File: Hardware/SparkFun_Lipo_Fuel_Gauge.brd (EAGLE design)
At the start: 10.2 x 24.1 mm, 17 parts, among them U2 MAX1704X

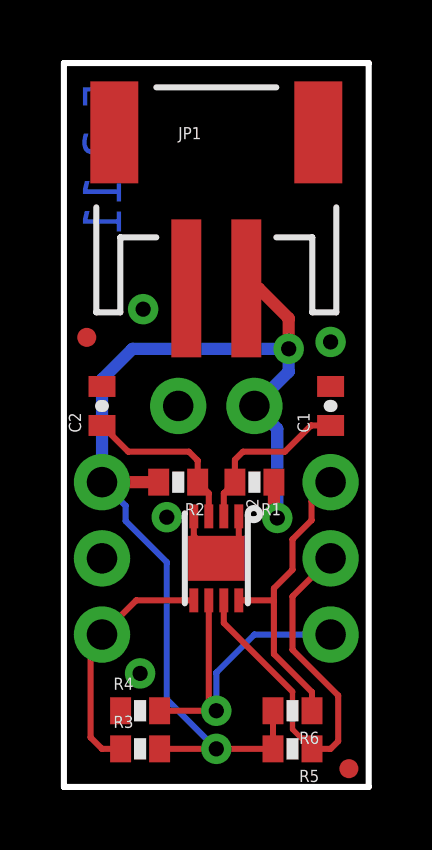
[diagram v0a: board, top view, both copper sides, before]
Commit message: Revision updates
Purpose of revision:
VCC connects directly to battery, which means a user could connect a 3V3 signal to 4V2 of the battery, causing things to break (see latest 1-star review on product page). This revision is to separate VCC from V_BATT, allowing users to use any voltage for the logic side. Also update to latest standards while we're at it.

Schematic changes:
Add Revised By
Update revision number
Replace VCC on battery side with V_BATT symbol
Separate regions of circuit
Add dashed lines to distinguish circuit regions
Separate JP1 and JP5
Replace schematic frame with current version
Replace "SFE" symbol with SparkFun logo
Move C2 to connect to VDD directly
Change flags to vector font
Change flags to correct types
Replace fiducials with new version

Board changes:
Add measures
Change copper date to version number
Add battery +/- labels to top silk
Add fiducials to bottom
Decrease GND pour isolation from 12mil to 8mil
Decrease all vias from 20 mil to 15 mil
Approve DRC keepout errors
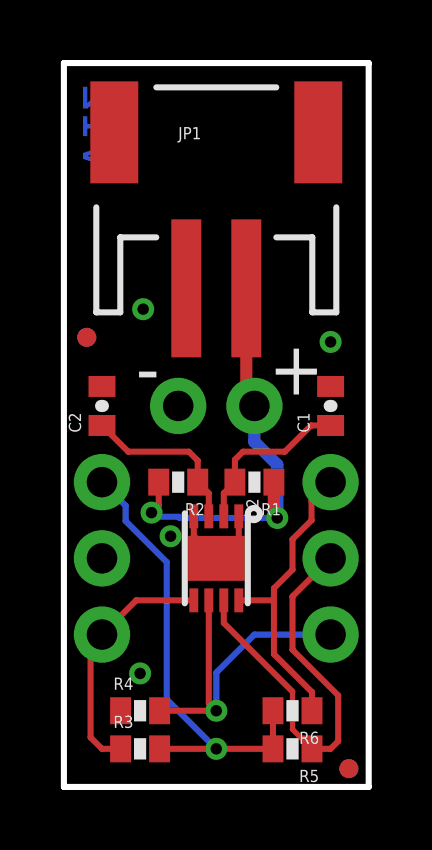
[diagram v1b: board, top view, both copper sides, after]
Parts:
- added FRAME1: FRAME-LETTER, SparkFun-Aesthetics:CREATIVE_COMMONS
- added JP8, JP9: FIDUCIALUFIDUCIAL, SparkFun-Aesthetics:FIDUCIAL-MICRO
- added LOGO1: SFE_LOGO_NAME_FLAMEBLANK, SparkFun-Aesthetics:BLANK
- JP3: value LOGO-SFESK -> SFE_LOGO_FLAME.1_INCH; device SparkFun:SFE-LOGO-FLAME -> SparkFun-Aesthetics:SFE_LOGO_FLAME_.1
- JP6, JP7: value FIDUCIAL1X2.5 -> FIDUCIALUFIDUCIAL; device abes:FIDUCIAL-1X2.5 -> SparkFun-Aesthetics:FIDUCIAL-MICRO
- moved JP3 1.66 mm to (5.08, 18.7)
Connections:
- new net V_BATT: JP1.2, JP5.1, R1.1, R2.2
- net VCC: no longer JP1.2, JP5.1, R1.1, R2.2
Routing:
- net VCC: track 38.1 -> 15.5 mm, vias 3 -> 1
- net V_BATT: track 0.00 -> 14.7 mm, vias 0 -> 2
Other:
- board text added: "Aaron Weiss"
- board text added: "Dryw Wade"
- board text added: "Revised by:"
- board text added: "v12"
- board text removed: "5-3-11"

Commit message: Design review updates
Schematic:
Replace old Eagle devices with current ones
Update MAX1704X symbol to match current standards
Add warning about single cell LiPo only
Add voltage range for V_BATT and VCC
Add I2C pullup isolation jumper

Board:
Fix routing with new footprints
Route straight out of all pads
Add vias to increase GND pour
Switch to Buzzard silk labels
Add units to measures
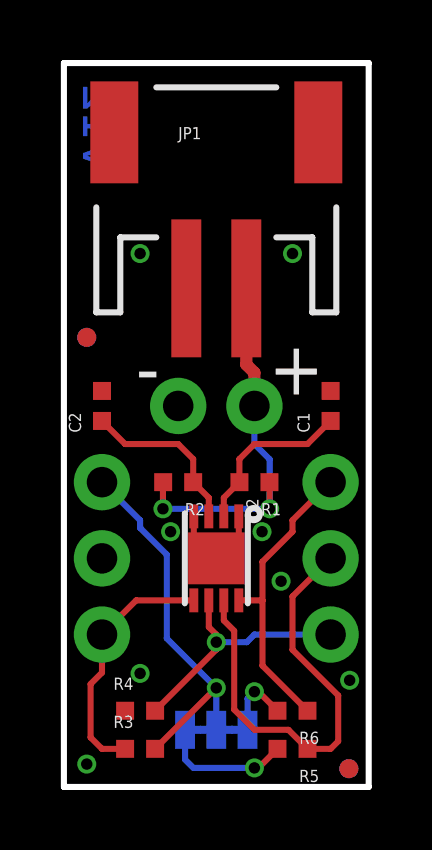
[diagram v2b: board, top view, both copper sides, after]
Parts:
- added I2C: JUMPER-SMT_3_2-NC_TRACE_SILK, SparkFun-Jumpers:SMT-JUMPER_3_2-NC_TRACE_SILK
- added U$2: (no value), output:#SDA#0
- added U$3: (no value), output:#SCL#0
- added U$4: (no value), output:#QST#0
- added U$5: (no value), output:#VCC#0
- added U$6: (no value), output:#GND#0
- added U$7: (no value), output:#ALT#0
- added U$8: (no value), output:#I2C#0
- C1: value 1uF -> 1.0uF; device SparkFun:0402-CAP -> SparkFun-Capacitors:0402-TIGHT
- C2: device SparkFun:0402-CAP -> SparkFun-Capacitors:0402-TIGHT
- JP1: device SparkFun:JST-2-SMD -> SparkFun-Connectors:JST-2-SMD
- JP2, JP4: device SparkFun:1X03 -> SparkFun-Connectors:1X03_NO_SILK
- JP5: device SparkFun:1X02 -> SparkFun-Connectors:1X02_NO_SILK
- R1: device SparkFun:0402-RES -> SparkFun-Resistors:0402-TIGHT
- R2: value 180 -> 100; device SparkFun:0402-RES -> SparkFun-Resistors:0402-TIGHT
- R3, R4, R5, R6: value 4.7k -> 2.2k; device SparkFun:0402-RES -> SparkFun-Resistors:0402-TIGHT
- U2: device SparkFun:TDFN-8 -> SparkFun-IC-Power:TDFN-8
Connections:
- new net N$1: I2C.3, R6.2
- new net N$3: I2C.1, R5.2
- net VCC: now also I2C.2; no longer R5.2, R6.2
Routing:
- net N$3: track 0.00 -> 4.45 mm, vias 0 -> 1
- net VCC: track 15.5 -> 12.7 mm
- net QST: track 11.3 -> 8.54 mm
- net N$1: track 0.00 -> 2.40 mm, vias 0 -> 1
- net V_BATT: track 14.7 -> 13.0 mm
- net SCL: track 14.4 -> 15.2 mm
- net GND: track 3.51 -> 3.38 mm, vias 4 -> 8
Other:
- board text added: "Units: inches"
- board text removed: "ALT"
- board text removed: "GND"
- board text removed: "QST"
- board text removed: "SCL"
- board text removed: "SDA"
- board text removed: "VCC"

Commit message: Silk change
Change Buzzard labels to non-pill style to fit larger text.
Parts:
- U$2: device output:#SDA#0 -> output:SDA0
- U$3: device output:#SCL#0 -> output:SCL0
- U$4: device output:#QST#0 -> output:QST0
- U$5: device output:#VCC#0 -> output:VCC0
- U$6: device output:#GND#0 -> output:GND0
- U$7: device output:#ALT#0 -> output:ALT0
- moved U$5 0.13 mm to (1.78, 10.2)
- moved U$6 0.13 mm to (1.78, 7.62)
- moved U$7 0.13 mm to (1.78, 5.08)
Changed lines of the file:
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@@
 <attribute name="VALUE" x="5.08" y="3.048" size="0.6096" layer="28" font="vector" ratio="20" rot="MR180" align="top-center"/>
 </element>
-<element name="U$2" library="output" package="#SDA#0" value="" x="8.255" y="10.16" smashed="yes" rot="MR0"/>
-<element name="U$3" library="output" package="#SCL#0" value="" x="8.255" y="7.62" smashed="yes" rot="MR0"/>
-<element name="U$4" library="output" package="#QST#0" value="" x="8.255" y="5.08" smashed="yes" rot="MR0"/>
-<element name="U$5" library="output" package="#VCC#0" value="" x="1.905" y="10.16" smashed="yes" rot="MR0"/>
-<element name="U$6" library="output" package="#GND#0" value="" x="1.905" y="7.62" smashed="yes" rot="MR0"/>
-<element name="U$7" library="output" package="#ALT#0" value="" x="1.905" y="5.08" smashed="yes" rot="MR0"/>
 <element name="U$8" library="output" package="#I2C#0" value="" x="3.556" y="1.905" smashed="yes" rot="MR0"/>
+<element name="U$2" library="output" package="SDA0" value="" x="8.255" y="10.16" smashed="yes" rot="MR0"/>
+<element name="U$3" library="output" package="SCL0" value="" x="8.255" y="7.62" smashed="yes" rot="MR0"/>
+<element name="U$4" library="output" package="QST0" value="" x="8.255" y="5.08" smashed="yes" rot="MR0"/>
+<element name="U$5" library="output" package="VCC0" value="" x="1.778" y="10.16" smashed="yes" rot="MR0"/>
+<element name="U$6" library="output" package="GND0" value="" x="1.778" y="7.62" smashed="yes" rot="MR0"/>
+<element name="U$7" library="output" package="ALT0" value="" x="1.778" y="5.08" smashed="yes" rot="MR0"/>
 </elements>
 <signals>
